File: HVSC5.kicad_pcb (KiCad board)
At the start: 2 copper layers, 240 x 152 mm, 360 parts, among them J1 test, J10 CONN_01X03, J11 test, J12 test, J13 test, J14 test, J15 test, J16 test, J17 CONN_COAXIAL, J18 CONN_01X03, J19 CONN_01X03, J2 test, J20 CONN_01X08, J21 test, J22 test, J23 test, J24 test, J25 CONN_01X05, J26 test, J27 test, J28 test, J29 test, J3 test, J4 test, J5 CONN_01X05, J6 test, J7 CONN_01X05, J8 CONN_COAXIAL, J9 DB9_Female_MountingHoles, SW1 SW_Push, SW3 SW_DPDT_x2, U1 AD7175-8, U10 LT1118-5V, U11 FOD0721, U12 DPBW06, U13 LTC2644, U14 uA7805, U15 INA128, U16 XR2206, U17 TLP176A, U18 ANA4522, U19 AQV258, U2 ADR4520, U20 AQV258, U21 ANA4522, U22 ANA4522, U3 ADR445, U4 74LS04, U5 dsPIC33EV256GM002, U6 SN75452, U7 MAX232, U8 HFBR-2412, U9 HFBR-1414, X1 P7002SCLRP, X2 P7002SCLRP, X3 P7002SCLRP, X4 P7002SCLRP, X5 P7002SCLRP, X6 P7002SCLRP, Y1 16M, Y2 8M

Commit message: High Voltage reinforce
고전압 부분 보강
AN2, AN3 두 부분 6.5V limit
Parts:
- added D15: SMDJ6.5CA, Diodes_SMD:D_SMC_Handsoldering, F.Cu at (29.0, 59.0)
- added D16: SMDJ6.5CA, Diodes_SMD:D_SMC_Handsoldering, F.Cu at (178.6, 98.6)
- added D25: SMDJ6.5CA, Diodes_SMD:D_SMC_Handsoldering, F.Cu at (171.7, 98.6)
- added R182: 300k, Resistors_THT:R_Axial_Power_L20.0mm_W6.4mm_P22.40mm, F.Cu at (37.8, 74.9)
- added R183: 51, Resistors_SMD:R_0805_HandSoldering, F.Cu at (190.5, 89.7)
- added R184: 51, Resistors_SMD:R_0805_HandSoldering, F.Cu at (190.5, 92.2)
- D8: value SMDJ6.5CA -> SMDJ100.5CA
- moved R163 37.6 mm to (213.5, 89.7), turned to 0 degrees
- moved D17 34.3 mm to (206.8, 89.7), turned to 0 degrees
- moved D8 25.1 mm to (29.0, 42.0)
- moved R32 11.2 mm to (37.8, 47.5)
- moved C68 5.08 mm to (165.9, 98.0)
- moved C69 5.08 mm to (162.1, 98.0)
- moved C70 5.08 mm to (148.8, 96.0)
- moved C71 5.08 mm to (165.9, 105.2)
- moved C72 5.08 mm to (162.1, 105.2)
- moved C73 5.08 mm to (148.8, 105.2)
- moved R176 5.08 mm to (161.0, 93.7)
- moved R177 5.08 mm to (156.0, 93.7)
- moved R178 5.08 mm to (156.0, 96.3)
- moved R180 5.08 mm to (153.4, 110.2)
- moved R181 5.08 mm to (153.4, 107.7)
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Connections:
- C60 pad 1: /ADC7175/AIN2 -> Net-(C60-Pad1)
- C61 pad 1: /ADC7175/AIN2 -> Net-(C60-Pad1)
- C62 pad 1: /ADC7175/AIN3 -> Net-(C62-Pad1)
- C63 pad 1: /ADC7175/AIN3 -> Net-(C62-Pad1)
- D8 pad 1: /Passive_Network/Monitor -> Net-(D8-Pad1)
- J26 pad 1: /ADC7175/AIN2 -> Net-(C60-Pad1)
- J27 pad 1: /ADC7175/AIN3 -> Net-(C62-Pad1)
- R168 pad 1: /ADC7175/AIN2 -> Net-(C60-Pad1)
- R169 pad 1: /ADC7175/AIN3 -> Net-(C62-Pad1)
- R32 pad 1: /Passive_Network/Monitor -> Net-(D8-Pad1)
- U21 pad 1: /ADC7175/AIN2 -> Net-(C60-Pad1)
- U21 pad 7: /ADC7175/AIN3 -> Net-(C62-Pad1)
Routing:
- net Net-(R163-Pad2): track 66.9 -> 15.0 mm
- net Net-(C62-Pad1): track 0.00 -> 48.7 mm, vias 0 -> 2
- net /ADC7175/AIN3: track 110.8 -> 75.1 mm
- net GNDREF: track 835.9 -> 868.9 mm
- net Net-(C60-Pad1): track 0.00 -> 24.8 mm, vias 0 -> 1
- net /ADC7175/AIN2: track 96.3 -> 75.4 mm
- net Net-(D8-Pad1): track 0.00 -> 20.5 mm
- net Net-(F2-Pad1): track 59.5 -> 72.6 mm
- net /Voltage_Divider/Monitor: track 148.0 -> 157.1 mm
- net Net-(J24-Pad1): track 28.6 -> 35.6 mm
- net Net-(D17-Pad1): track 65.1 -> 59.8 mm, vias 0 -> 1
- net Net-(F3-Pad1): track 97.8 -> 102.8 mm
- net /ADC7175/AIN8: track 79.1 -> 83.9 mm
- net /Monitor/Sine_ON: track 111.2 -> 114.7 mm
- net /ADC7175/AIN9: track 79.7 -> 76.6 mm
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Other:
- board text added: "High Voltage Signal Conditioner Version 1.4 04/07/2018, Designed by JHENG"
- board text removed: "High Voltage Signal Conditioner Version 1.3 18/06/2018, Designed by JHENG"

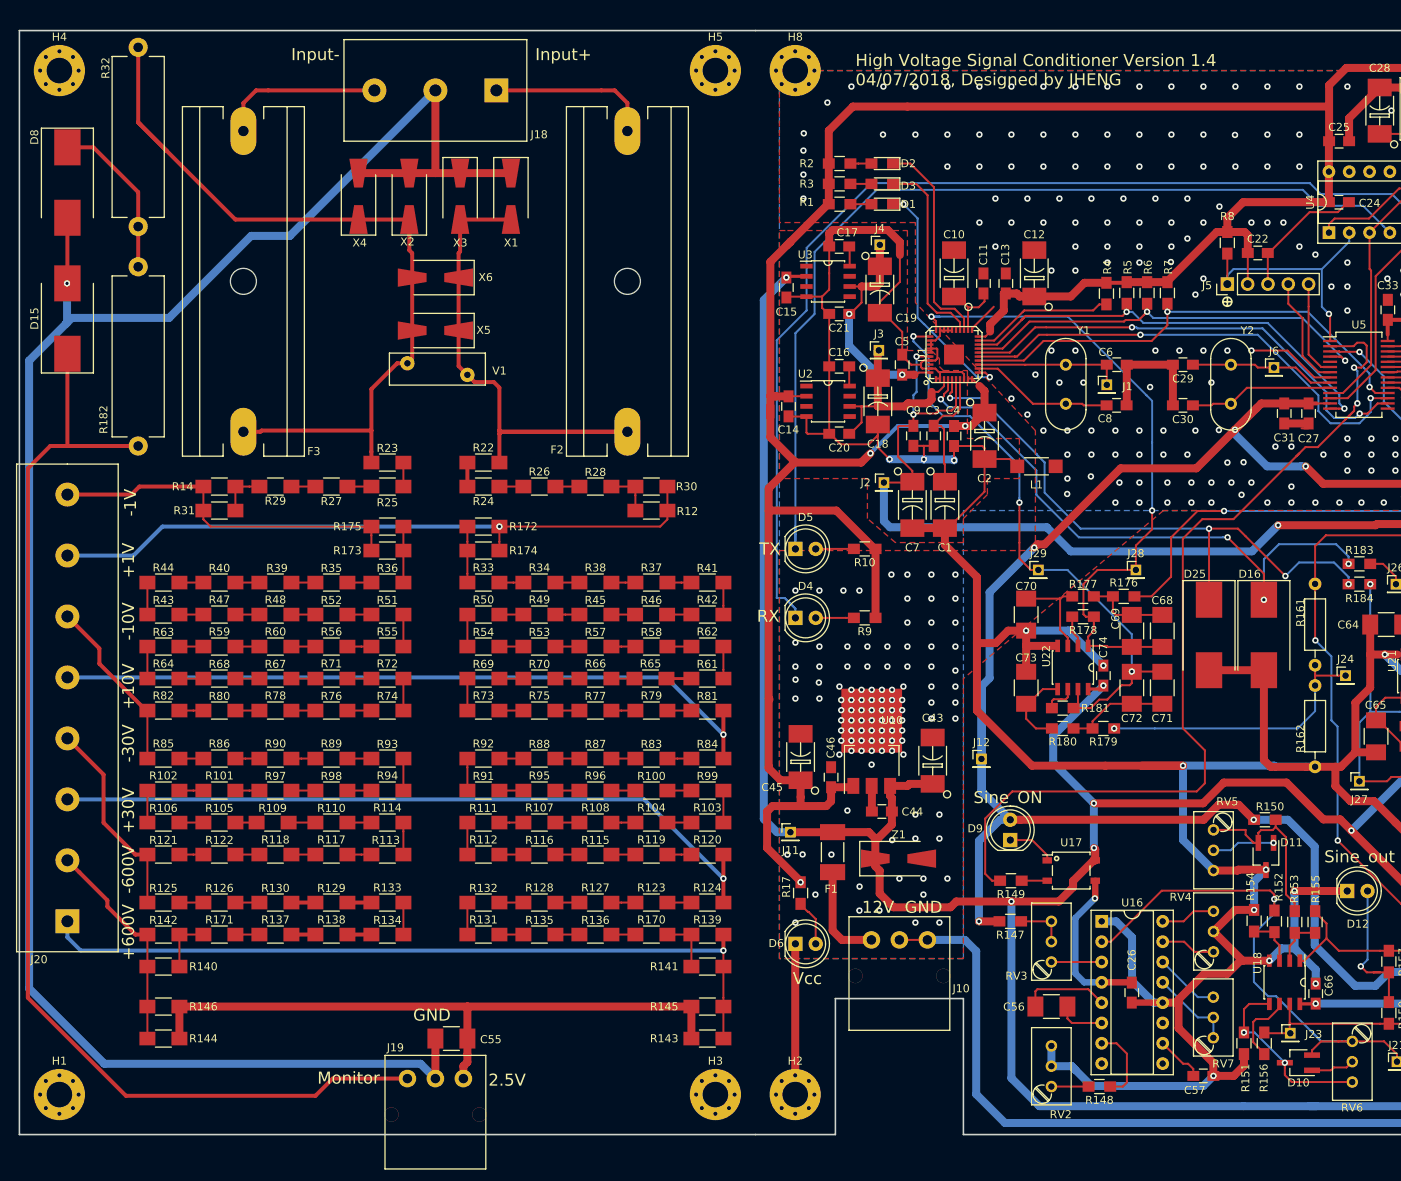
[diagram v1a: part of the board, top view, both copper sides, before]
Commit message: 3차 PCB
1. 모니터 고압부 150k옴 2갤로 수정
2. 6.5V Zener 추가
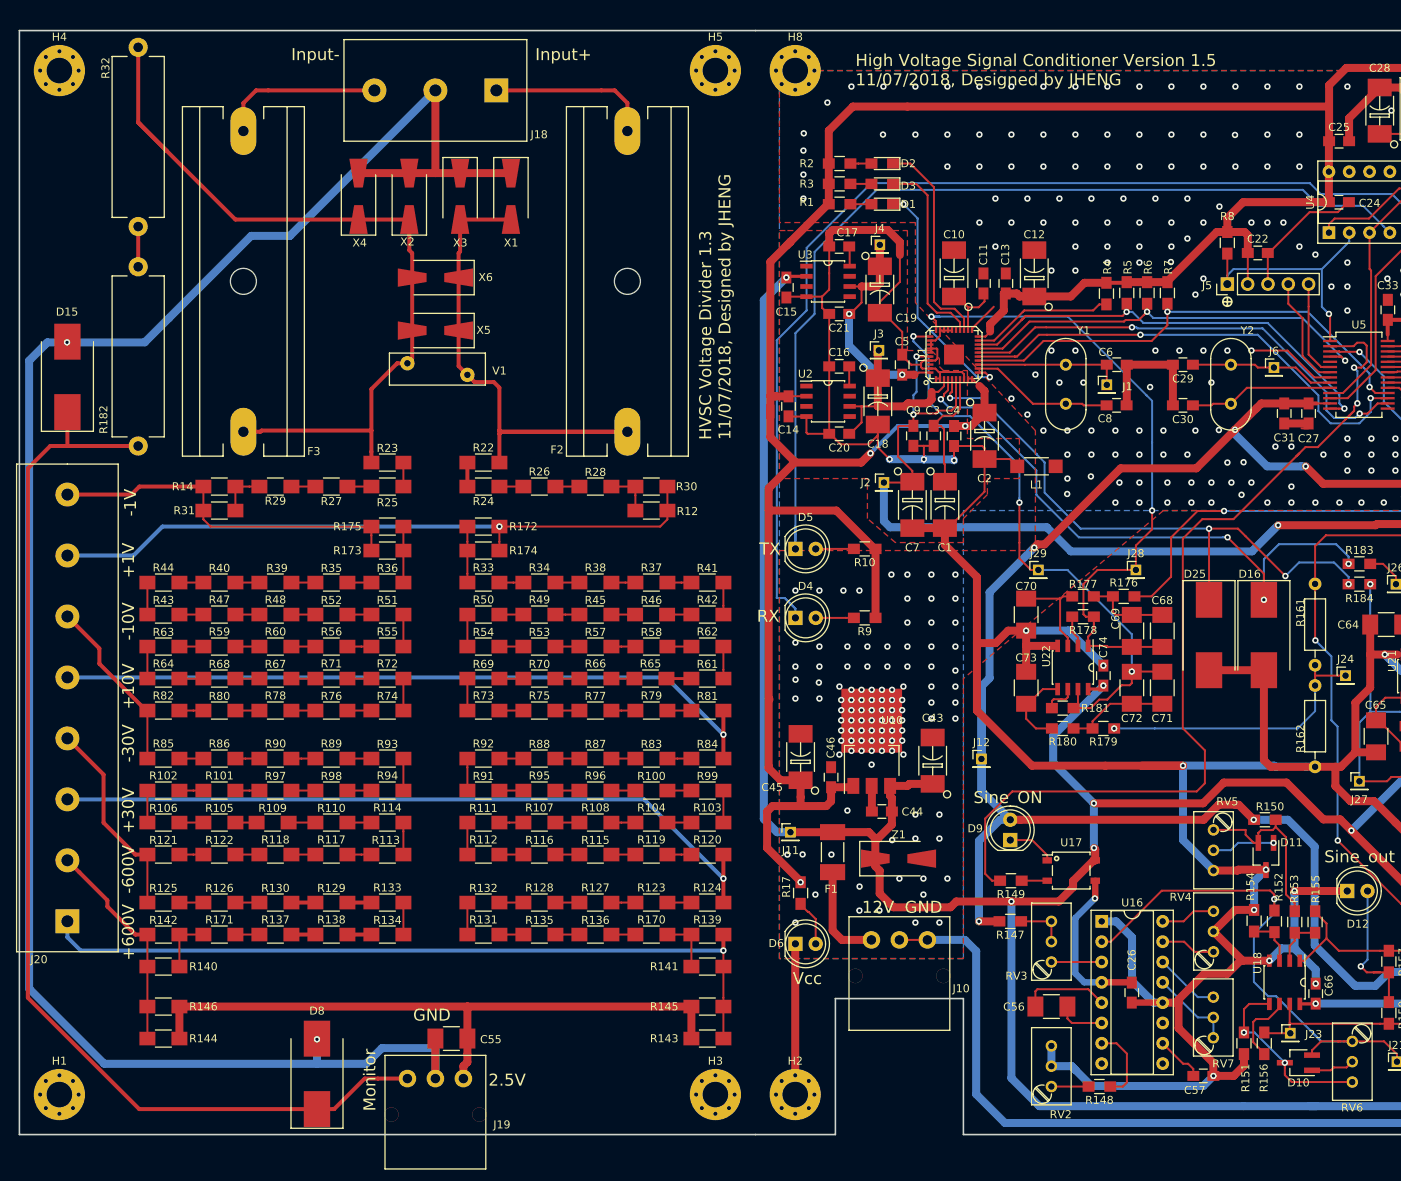
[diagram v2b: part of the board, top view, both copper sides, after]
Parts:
- moved D8 115.7 mm to (60.2, 153.4), turned to 90 degrees
- moved D15 7.29 mm to (29.0, 66.3)
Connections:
- D8 pad 1: Net-(D8-Pad1) -> /Passive_Network/Monitor
- R182 pad 2: Net-(D8-Pad1) -> Net-(R182-Pad2)
- R32 pad 1: Net-(D8-Pad1) -> Net-(R182-Pad2)
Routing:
- net Net-(D8-Pad1): track 20.5 -> 0.00 mm
- net GNDREF: track 868.9 -> 862.5 mm, vias 20 -> 21
- net /Passive_Network/Monitor: track 146.1 -> 140.2 mm
- net Net-(R182-Pad2): track 0.00 -> 5.03 mm
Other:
- board text added: "HVSC Voltage Divider 1.3 11/07/2018, Designed by JHENG"
- board text added: "High Voltage Signal Conditioner Version 1.5 11/07/2018, Designed by JHENG"
- board text removed: "High Voltage Signal Conditioner Version 1.4 04/07/2018, Designed by JHENG"

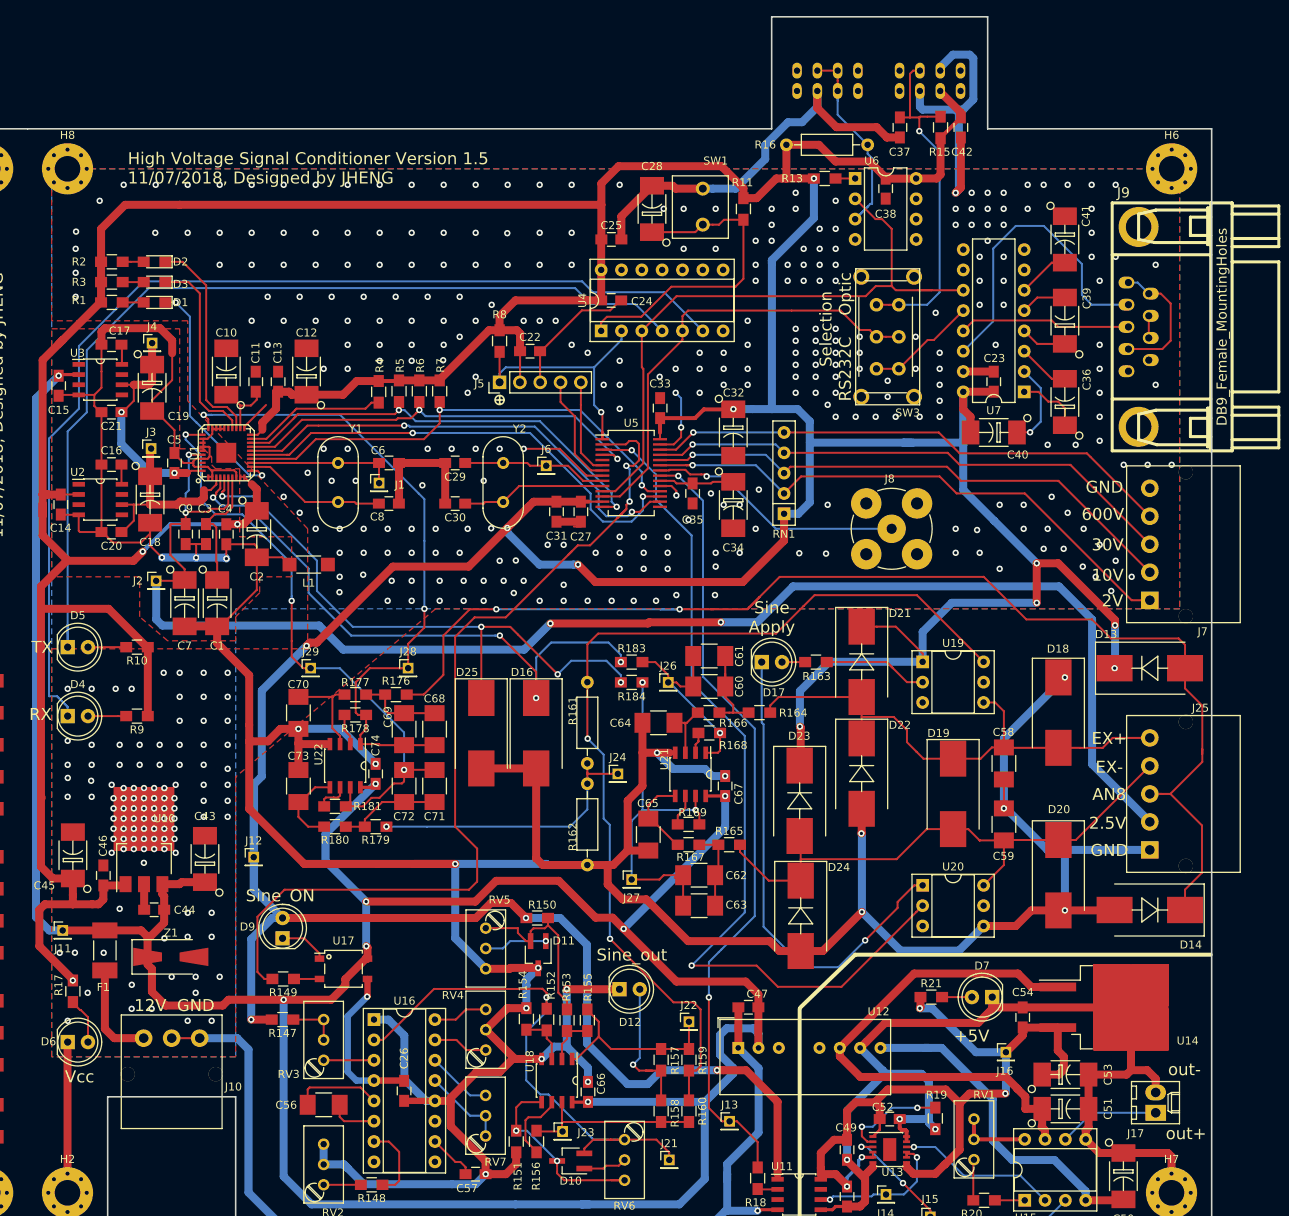
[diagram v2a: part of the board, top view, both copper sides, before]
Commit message: 4차 PCB
U23 Wire Breakage Relay 추가
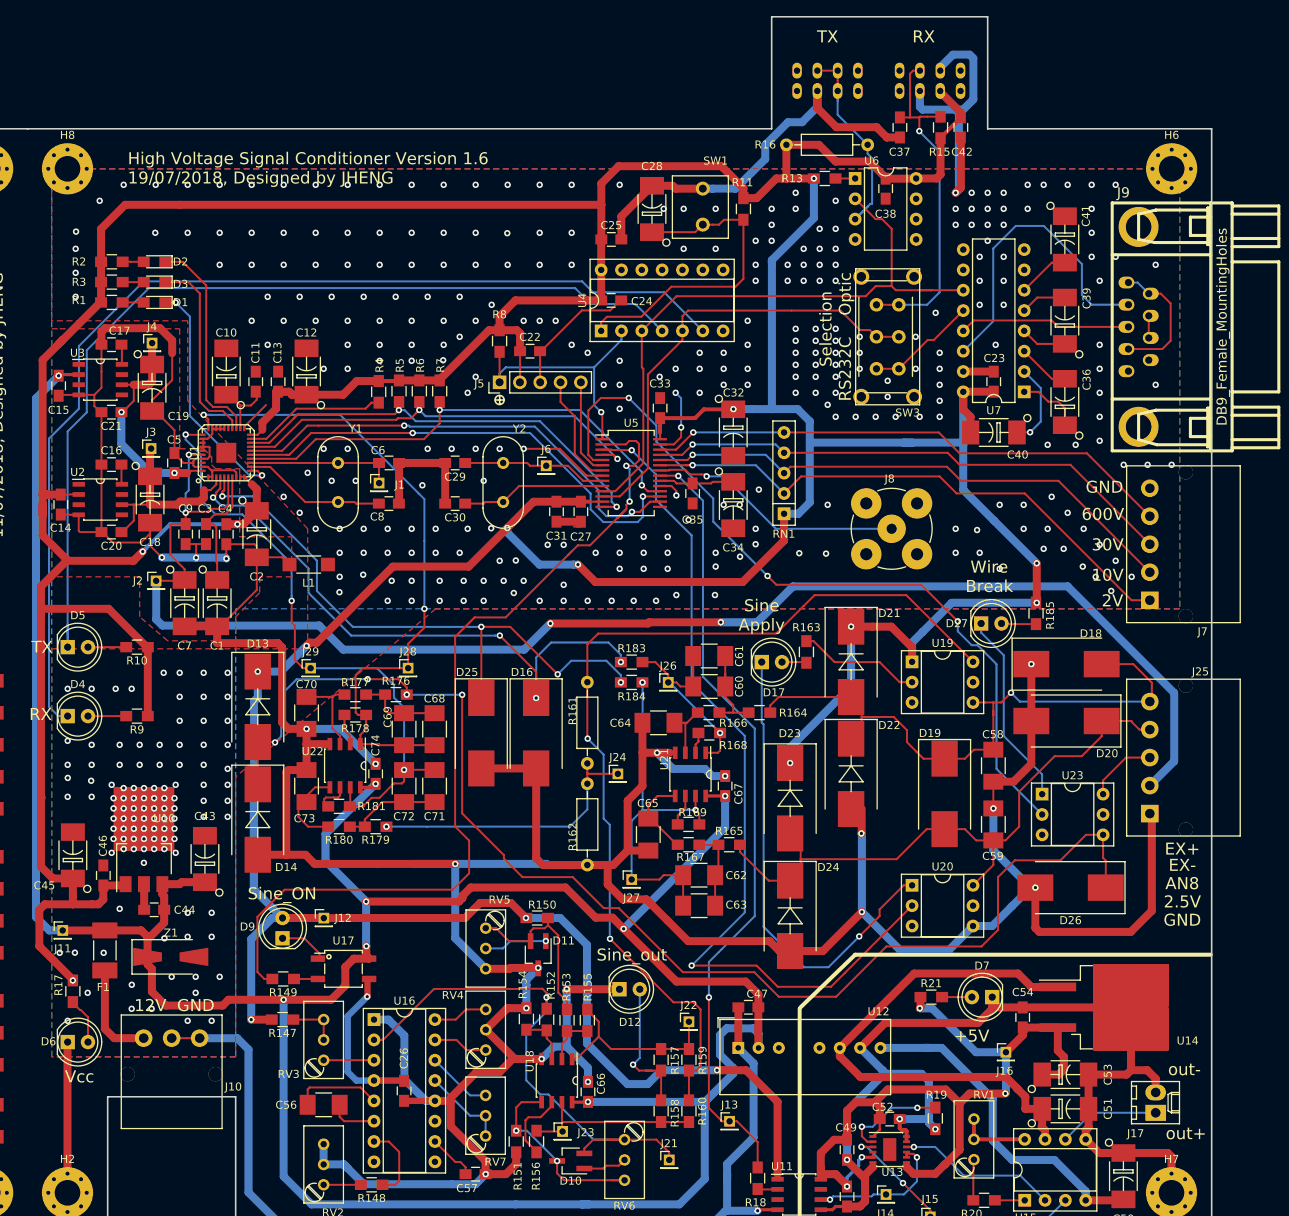
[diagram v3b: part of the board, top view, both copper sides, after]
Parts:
- added D26: SMDJ6.5CA, Diodes_SMD:D_SMC_Handsoldering, F.Cu at (245.4, 117.9)
- added D27: LED, LEDs:LED_D5.0mm, F.Cu at (234.2, 84.8)
- added R185: 100, Resistors_SMD:R_0805_HandSoldering, F.Cu at (241.0, 83.6)
- added U23: AQV258, Housings_DIP:DIP-6_W7.62mm_Socket, F.Cu at (241.8, 106.2)
- C60, C61: value 22uF -> 0.47uF
- C62, C63: value 20uF -> 0.47uF
- D18, D19, D20: value SMDJ6.5CA -> SMDJ10
- D8: value SMDJ100.5CA -> SMDJ6.5CA
- R182, R32: value 300k -> 150k
- U17: footprint Housings_SOIC:SO-4_4.4x4.3mm_Pitch2.54mm -> USER:SO-4_4.4x4.3mm_Pitch2.54mm_Hand_Soldering
- moved D14 112.1 mm to (143.8, 109.3), turned to 270 degrees
- moved D13 111.6 mm to (143.8, 95.2), turned to 270 degrees
- moved D20 19.3 mm to (244.9, 97.0), turned to 180 degrees
- moved J12 11.6 mm to (152.0, 121.7)
- moved D18 6.15 mm to (244.9, 89.9), turned to 0 degrees
- moved J25 4.54 mm to (255.3, 101.6)
- moved R163 1.74 mm to (212.3, 88.4), turned to 90 degrees
- moved C58 1.35 mm to (235.7, 102.6)
- moved D22 1.32 mm to (217.9, 103.6)
- moved C59 1.32 mm to (235.7, 110.0)
- moved D21 1.32 mm to (217.9, 89.6)
- moved U19 1.32 mm to (225.6, 89.6)
- moved U20 1.32 mm to (225.6, 117.6)
- moved D24 1.32 mm to (210.3, 121.4)
- moved D23 1.23 mm to (210.3, 106.7)
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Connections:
- D13 pad 2: /Voltage_Divider/Monitor -> /Voltage_Divider/MonitorP
- D14 pad 1: /Voltage_Divider/Monitor -> /Voltage_Divider/MonitorP
- R176 pad 2: /Voltage_Divider/Monitor -> /Voltage_Divider/MonitorP
- U20 pad 2: /Voltage_Divider/Wire_Break -> /Voltage_Divider/Sine_APP
- U5 pad 3: /Voltage_Divider/Wire_Break -> /Voltage_Divider/Sine_APP
- U5 pad 5: Net-(U5-Pad5) -> /Voltage_Divider/Wire_Break
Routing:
- net /Voltage_Divider/MonitorP: track 0.00 -> 162.2 mm, vias 0 -> 4
- net /Voltage_Divider/Monitor: track 157.1 -> 8.99 mm, vias 2 -> 0
- net /Voltage_Divider/Sine_APP: track 0.00 -> 109.6 mm, vias 0 -> 2
- net Net-(D27-Pad1): track 0.00 -> 24.5 mm
- net VCC: track 904.4 -> 886.9 mm
- net /Voltage_Divider/Wire_Break: track 110.9 -> 97.8 mm, vias 2 -> 3
- net /Voltage_Divider/Excite+: track 65.7 -> 77.2 mm, vias 0 -> 1
- net GNDREF: track 862.5 -> 854.8 mm
- net /Voltage_Divider/Excite-: track 71.5 -> 78.2 mm
- net Net-(D27-Pad2): track 0.00 -> 4.35 mm
- net /ADC7175/AIN9: track 76.6 -> 79.3 mm
- net /Monitor/Sine_ON: track 114.7 -> 112.7 mm
- net +2V5: track 270.4 -> 269.0 mm
- net /Monitor/Sine: track 121.0 -> 119.7 mm
- net Net-(D17-Pad1): track 59.8 -> 58.6 mm
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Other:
- net class Default: clearance 0 -> 0.15
- rule trace_clearance: 0 -> 0.15
- board text added: "High Voltage Signal Conditioner Version 1.6 19/07/2018, Designed by JHENG"
- board text added: "Wire Break"
- board text removed: "High Voltage Signal Conditioner Version 1.5 11/07/2018, Designed by JHENG"

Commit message: Balanced Resistor 추가
D28 D29, R186, R187 추가
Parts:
- added D28: SMDJ11CA, Diodes_SMD:D_SMC_Handsoldering, F.Cu at (104.5, 40.6)
- added D29: SMDJ11CA, Diodes_SMD:D_SMC_Handsoldering, F.Cu at (111.5, 40.6)
- added R186: 150k, Resistors_THT:R_Axial_Power_L20.0mm_W6.4mm_P22.40mm, F.Cu at (111.0, 73.0)
- added R187: 150k, Resistors_THT:R_Axial_Power_L20.0mm_W6.4mm_P22.40mm, F.Cu at (111.0, 99.0)
- D15, D8: value SMDJ6.5CA -> SMDJ11CA
- moved R32 6.08 mm to (31.8, 48.5)
- moved C55 6.00 mm to (71.0, 149.0)
- moved D15 6.00 mm to (23.0, 66.3)
- moved D8 6.00 mm to (54.2, 153.4)
- moved F2 6.00 mm to (93.0, 73.2)
- moved F3 6.00 mm to (45.0, 73.2)
- moved H1 6.00 mm to (22.0, 156.0)
- moved H3 6.00 mm to (104.0, 156.0)
- moved H4 6.00 mm to (22.0, 28.0)
- moved H5 6.00 mm to (104.0, 28.0)
- moved J18 6.00 mm to (69.0, 30.5)
- moved J19 6.00 mm to (69.0, 154.0)
- moved J20 6.00 mm to (23.0, 126.7)
- moved R100 6.00 mm to (96.0, 118.0)
- moved R101 6.00 mm to (42.0, 118.0)
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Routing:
- net GNDREF: track 854.8 -> 907.4 mm
- net Net-(F2-Pad1): track 72.6 -> 109.9 mm
- net Net-(D28-Pad1): track 0.00 -> 14.8 mm
- net Net-(R186-Pad1): track 0.00 -> 3.60 mm
- net /Voltage_Divider/Monitor: track 8.99 -> 11.8 mm
- net /Voltage_Divider/Excite-: track 78.2 -> 79.4 mm
- net Net-(R182-Pad2): track 5.03 -> 4.03 mm
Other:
- board size 240 x 152 mm -> 246 x 152 mm
- board text added: "HVSC Voltage Divider 1.4 23/07/2018, Designed by JHENG"
- board text added: "MOM"
- board text removed: "AN8"
- board text removed: "HVSC Voltage Divider 1.3 11/07/2018, Designed by JHENG"
